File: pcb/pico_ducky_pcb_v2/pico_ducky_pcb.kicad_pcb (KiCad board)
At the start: 4 copper layers, 14 x 30 mm, 31 parts, among them J1 USB_A, SW1 R-667799, SW2 R-667799, U1 MIC5504-3.3YMT, U2 W25Q32JVZP, U3 RP2040, Y1 Crystal_GND24

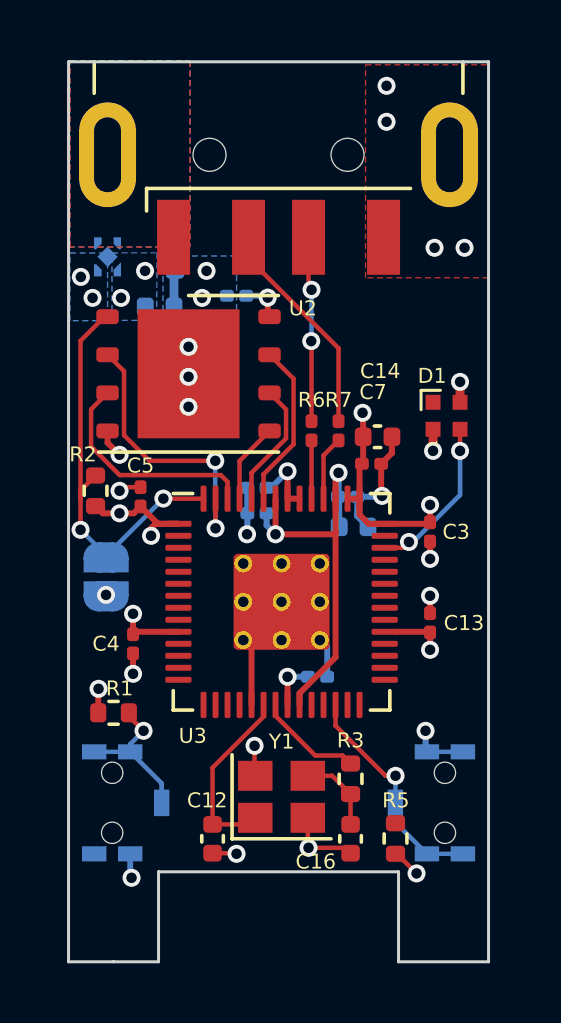
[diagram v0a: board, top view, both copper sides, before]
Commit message: update the R-667799 footprint and component finish routing
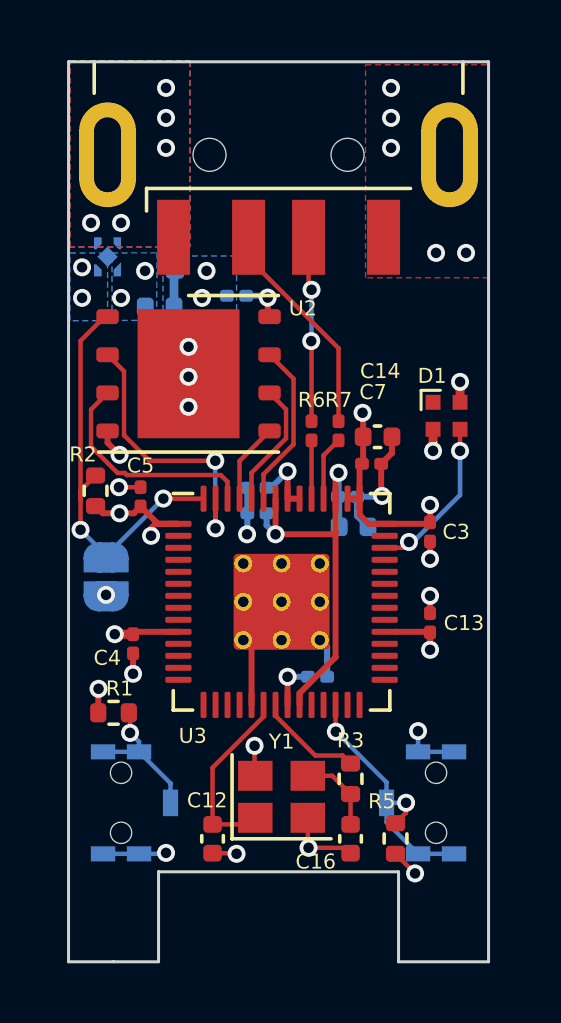
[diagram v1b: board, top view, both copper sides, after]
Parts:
- SW1, SW2: value R-667799 -> SW_SPST_GND; footprint R-WHATEVER:R-667799 -> pico-ducky-pcb-v2:R-667799
- moved SW1 0.55 mm to (81.8, 64.7)
- moved SW2 0.55 mm to (92.2, 64.7)
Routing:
- net GND: track 21.8 -> 23.1 mm, vias 25 -> 26
- net /RESET: track 7.62 -> 8.78 mm, vias 1 -> 2
- net +5V: vias 0 -> 5

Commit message: add silk screen
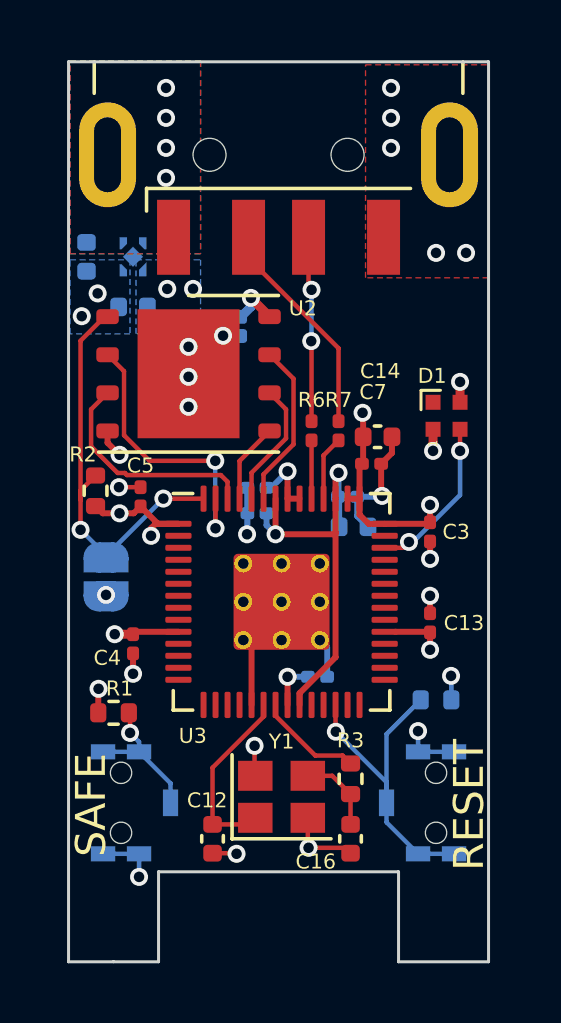
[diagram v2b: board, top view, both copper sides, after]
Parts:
- added REF**: OSHW-Logo2_7.3x6mm_SilkScreen, Symbol:OSHW-Logo2_7.3x6mm_SilkScreen, B.Cu at (87.0, 44.6)
- R5: moved to B.Cu
- moved R5 4.81 mm to (92.2, 61.3), turned to 180 degrees
- moved C1 2.95 mm to (80.6, 46.5)
- moved C10 1.03 mm to (85.8, 48.8), turned to 90 degrees
- moved C6 0.89 mm to (82.2, 48.2), turned to 0 degrees
- moved U1 0.85 mm to (82.2, 46.5)
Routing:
- net /RESET: track 8.78 -> 11.2 mm, vias 2 -> 1
- net GND: track 23.1 -> 22.3 mm, vias 26 -> 25
- net +5V: vias 5 -> 4
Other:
- board text added: "BOOT SEL"
- board text added: "Kevin Lutzer"
- board text added: "RESET"
- board text added: "RP Duck V2"
- board text added: "SAFE"

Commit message: pico duck
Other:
- board text added: "BOOT"
- board text added: "SEL"
- board text removed: "BOOT SEL"
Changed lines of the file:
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@@
   (gr_line (start 83 70) (end 83 67) (layer "Edge.Cuts") (width 0.1))
   (gr_line (start 94 70) (end 94 40) (layer "Edge.Cuts") (width 0.1))
-  (gr_text "BOOT SEL" (at 82.95 58.47 270) (layer "B.SilkS")
+  (gr_text "SEL" (at 82.85 57.17 270) (layer "B.SilkS")
     (effects (font (size 1 1) (thickness 0.15)) (justify mirror))
   )
-  (gr_text "RP Duck V2" (at 84.35 57.97 270) (layer "B.SilkS")
+  (gr_text "BOOT" (at 84.05 57.27 270) (layer "B.SilkS")
+    (effects (font (size 1 1) (thickness 0.15)) (justify mirror))
+  )
+  (gr_text "RP Duck\nV2" (at 83.75 60.57 270) (layer "B.SilkS")
     (effects (font (size 1 1) (thickness 0.15)) (justify right mirror))
   )

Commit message: more silkscreen cleanup{
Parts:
- removed REF**: OSHW-Logo2_7.3x6mm_SilkScreen, Symbol:OSHW-Logo2_7.3x6mm_SilkScreen
- moved R7 0.10 mm to (88.9, 52.3)
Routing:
- net GND: track 22.3 -> 22.2 mm, vias 25 -> 28

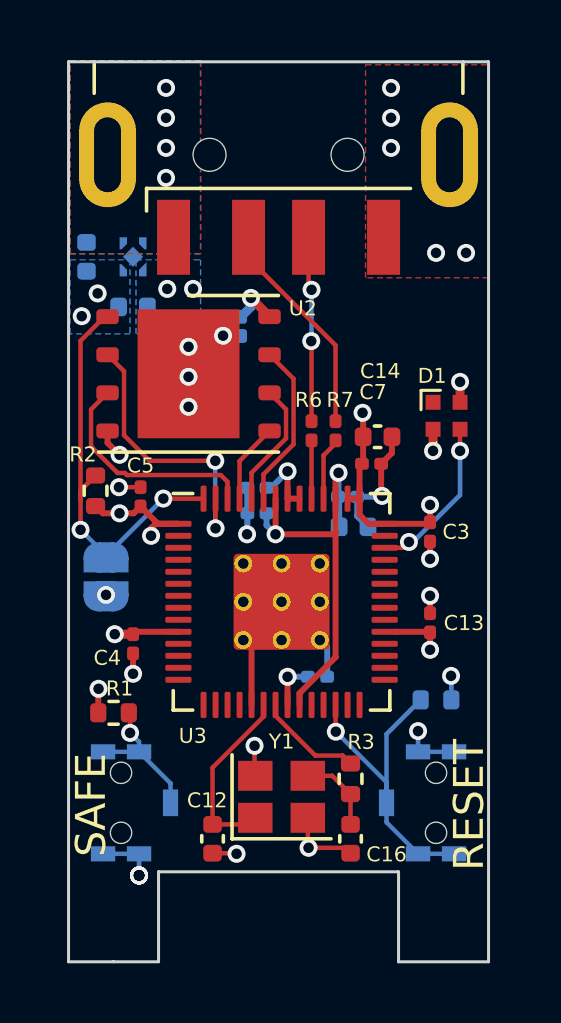
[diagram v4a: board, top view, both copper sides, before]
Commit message: use the weurth usb a connector
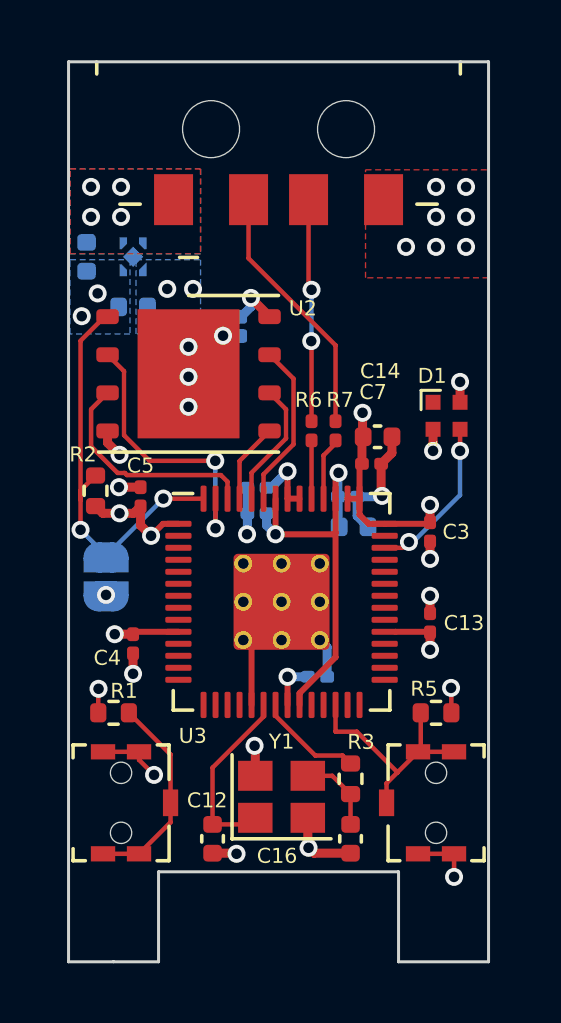
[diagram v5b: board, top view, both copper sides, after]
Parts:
- J1: footprint Connector_USB:USB_A_CNCTech_1001-011-01101_Horizontal -> pico-ducky-pcb-v2:USB3_A_Plug_Wuerth_629004113921_Horizontal
- R5, SW1, SW2: moved to F.Cu
- moved J1 6.17 mm to (82.2, 40.0)
- moved R5 0.43 mm to (92.2, 61.7)
- turned SW1 to -90 degrees
- turned SW2 to 90 degrees
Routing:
- net /RESET: track 11.2 -> 8.22 mm, vias 1 -> 0
- net /SAFE_BOOT: track 4.78 -> 6.91 mm, vias 1 -> 0
- net GND: track 22.2 -> 24.1 mm, vias 28 -> 27
- net +1V1: track 14.2 -> 16.0 mm
- net /USB_-: track 7.33 -> 8.59 mm
- net /USB_+: track 6.18 -> 7.44 mm
- net +3V3: track 24.6 -> 23.9 mm
